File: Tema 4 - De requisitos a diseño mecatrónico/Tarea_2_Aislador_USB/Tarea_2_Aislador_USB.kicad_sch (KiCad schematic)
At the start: 24 parts, among them IC1 ADUM3160BRWZ, IC2 NUP2202W1T2G, IC3 NUP2202W1T2G, IC4 ADUM5000ARWZ, J1 87520-0010BLF, J2 USB-B-S-F-B-TH-R

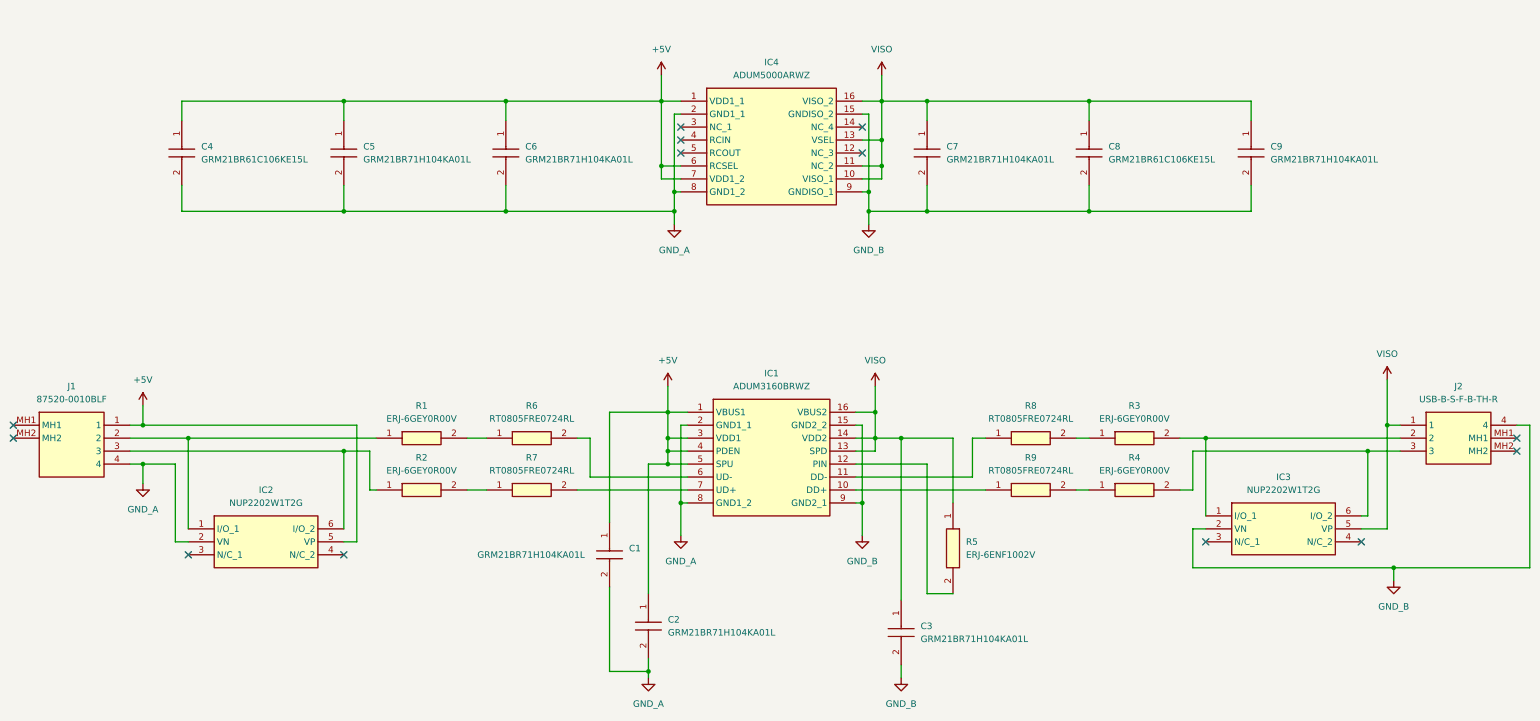
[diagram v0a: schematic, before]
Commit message: PCB de la tarea 2 finalizado
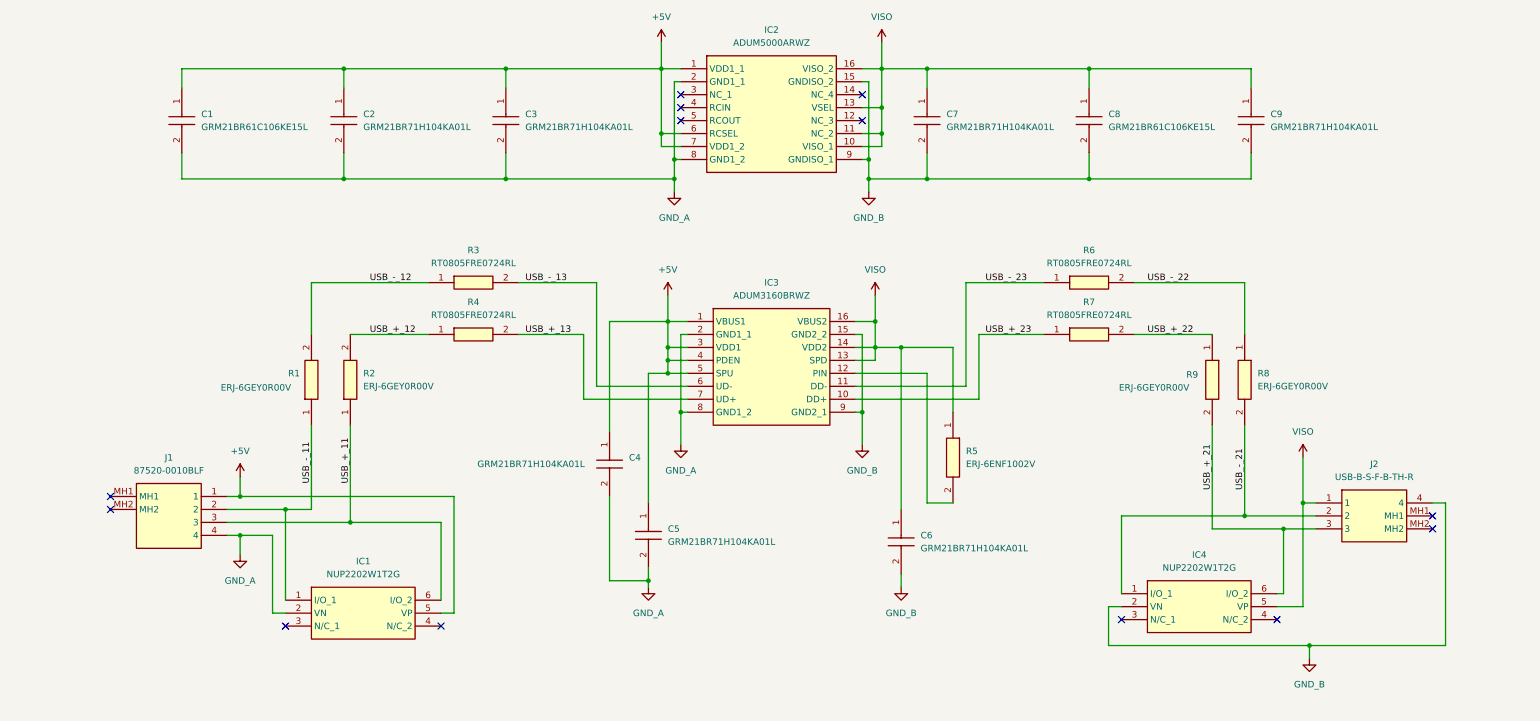
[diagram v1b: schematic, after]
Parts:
- renumbered C4 to C1, C5 to C2, C6 to C3, C1 to C4, C2 to C5, C3 to C6, IC2 to IC1, IC4 to IC2, IC1 to IC3, IC3 to IC4, R6 to R3, R7 to R4, R8 to R6, R9 to R7, R3 to R8, R4 to R9
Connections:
- net USB_-_11: now reaches IC1.1 (I/O_1), J1.2, R1.1
- net USB_-_12: now reaches R1.2, R3.1
- net USB_+_11: now reaches IC1.6 (I/O_2), J1.3, R2.1
- net USB_-_13: now reaches IC3.6 (UD-), R3.2
- net USB_+_12: now reaches R2.2, R4.1
- net USB_+_23: now reaches IC3.10 (DD+), R7.1
- net USB_-_23: now reaches IC3.11 (DD-), R6.1
- net USB_+_13: now reaches IC3.7 (UD+), R4.2
- net USB_-_22: now reaches R6.2, R8.1
- net USB_-_21: now reaches IC4.1 (I/O_1), J2.2, R8.2
- net USB_+_21: now reaches IC4.6 (I/O_2), J2.3, R9.2
- net USB_+_22: now reaches R7.2, R9.1
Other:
- moved on the sheet: C1, C2, C3, C4, C5, C6, C7, C8, C9, IC1, IC2, IC3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

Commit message: Actualización del aislador USB
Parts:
- added D1: Green, PCM_JLCPCB:D_0603, symbol PCM_JLCPCB-Diodes:LED,0603,Green
- added R10: 100Ω, PCM_JLCPCB:R_0603, symbol PCM_JLCPCB-Resistors:0603,100Ω
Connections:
- net +5V: now also R10.1
- net GND_A: now also J1.MH1, J1.MH2, D1.1
- net GND_B: now also J2.MH1, J2.MH2
- new net: D1.2, R10.2
- no-connect marks 13 -> 9
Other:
- moved on the sheet: C1, C2, C3, C4, C5, C6, C7, C8, C9, IC1, IC2, IC3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
